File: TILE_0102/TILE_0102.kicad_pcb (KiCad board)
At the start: 2 copper layers, 42.1 x 24.6 mm, 3 parts

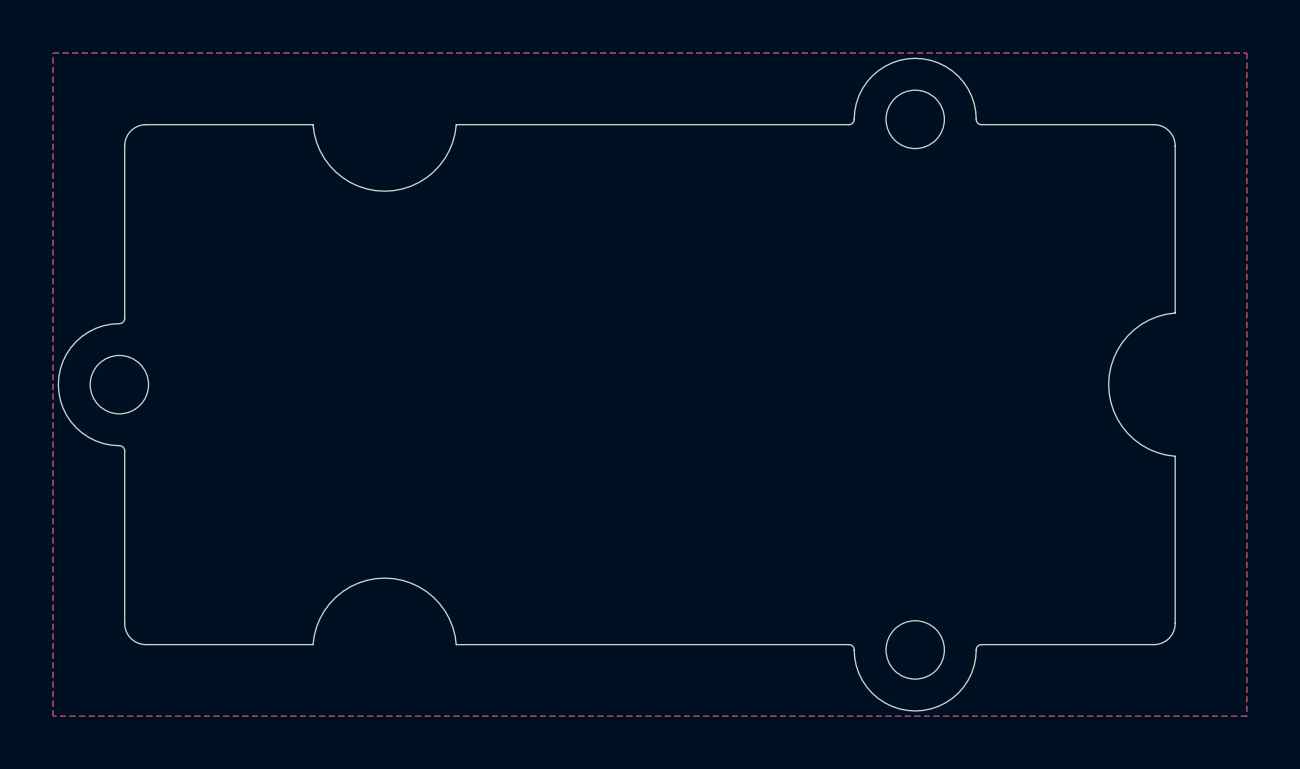
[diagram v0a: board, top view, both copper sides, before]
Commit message: Migrate to KiCad 6
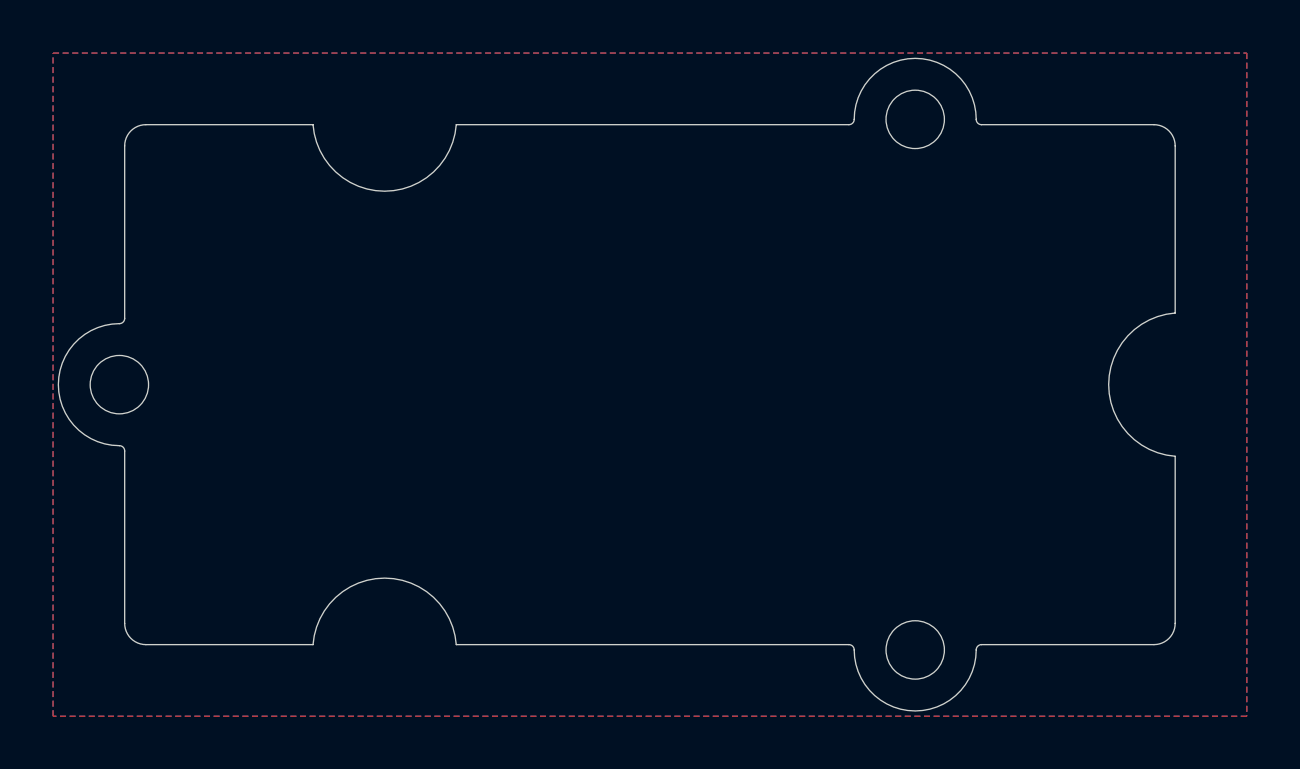
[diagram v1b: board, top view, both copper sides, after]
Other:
- net class Default removed
- net class RF removed
- net class VCC removed
